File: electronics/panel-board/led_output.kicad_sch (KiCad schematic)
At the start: 12 parts, among them J17 Conn_02x04_Odd_Even, U11 74HCT245

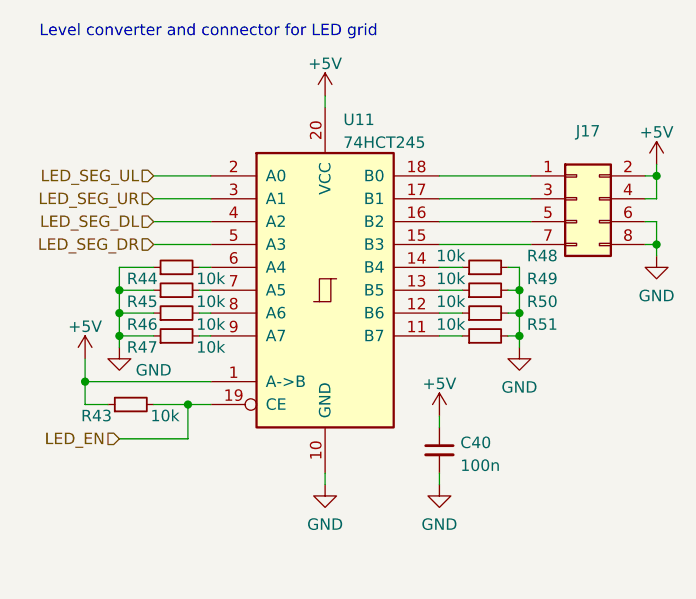
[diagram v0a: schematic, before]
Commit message: Update PadBUS standard
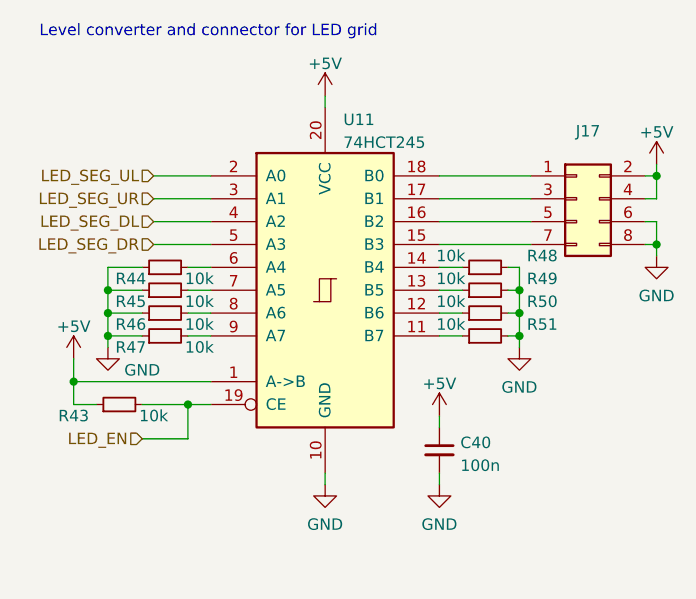
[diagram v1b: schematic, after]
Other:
- moved on the sheet: R43, R44, R45, R46, R47

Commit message: Pre LED grid changes
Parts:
- added H3, H4: MountingHole_Pad, MountingHole:MountingHole_3.2mm_M3_Pad, symbol Mechanical:MountingHole_Pad
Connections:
- no-connect marks 0 -> 2
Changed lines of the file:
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@@
   (junction (at 74.93 46.99) (diameter 0) (color 0 0 0 0)
   )
+  (no_connect (at 25.4 76.2))
+  (no_connect (at 33.02 76.2))
   (wire (pts (xy 74.93 41.91) (xy 74.93 44.45))
     (stroke (width 0) (type default) (color 0 0 0 0))
@@
     (pin "2")
   )
+  (symbol (lib_id "Mechanical:MountingHole_Pad") (at 33.02 73.66 0) (mirror y) (unit 1)
+    (in_bom yes) (on_board yes) (fields_autoplaced)
+    (property "Reference" "H4" (id 0) (at 30.48 71.5553 0)
+      (effects (font (size 1.27 1.27)) (justify left))
+    )
+    (property "Value" "MountingHole_Pad" (id 1) (at 30.48 74.0922 0)
+      (effects (font (size 1.27 1.27)) (justify left) hide)
+    )
+    (property "Footprint" "MountingHole:MountingHole_3.2mm_M3_Pad" (id 2) (at 33.02 73.66 0)
+      (effects (font (size 1.27 1.27)) hide)
+    )
+    (property "Datasheet" "~" (id 3) (at 33.02 73.66 0)
+      (effects (font (size 1.27 1.27)) hide)
+    )
+    (pin "1")
+  )
   (symbol (lib_id "power:GND") (at 90.17 40.64 0) (unit 1)
     (in_bom yes) (on_board yes) (fields_autoplaced)
@@
     )
     (property "Datasheet" "" (id 3) (at 53.34 22.86 0)
+      (effects (font (size 1.27 1.27)) hide)
+    )
+    (pin "1")
+  )
+  (symbol (lib_id "Mechanical:MountingHole_Pad") (at 25.4 73.66 0) (mirror y) (unit 1)
+    (in_bom yes) (on_board yes) (fields_autoplaced)
+    (property "Reference" "H3" (id 0) (at 22.86 71.5553 0)
+      (effects (font (size 1.27 1.27)) (justify left))
+    )
+    (property "Value" "MountingHole_Pad" (id 1) (at 22.86 74.0922 0)
+      (effects (font (size 1.27 1.27)) (justify left) hide)
+    )
+    (property "Footprint" "MountingHole:MountingHole_3.2mm_M3_Pad" (id 2) (at 25.4 73.66 0)
+      (effects (font (size 1.27 1.27)) hide)
+    )
+    (property "Datasheet" "~" (id 3) (at 25.4 73.66 0)
       (effects (font (size 1.27 1.27)) hide)
     )
@@
     (pin "1")
   )
+  (sheet_instances
+    (path "/" (page "1"))
+  )
+  (symbol_instances
+    (path "/461e0b65-0fb8-4924-9a86-ecf473ffba58"
+      (reference "#PWR096") (unit 1) (value "+5V") (footprint "")
+    )
+    (path "/277de0f0-3211-4bd1-b44f-edce4479dc5e"
+      (reference "#PWR097") (unit 1) (value "GND") (footprint "")
+    )
+    (path "/9244ab2d-6ee8-49fa-9ad3-e2a4e003c7fc"
+      (reference "#PWR098") (unit 1) (value "+5V") (footprint "")
+    )
+    (path "/18e83fbf-8ee7-4c40-a225-e25221b68051"
+      (reference "#PWR099") (unit 1) (value "GND") (footprint "")
+    )
+    (path "/2f5e3d2b-d1ac-4ed0-925a-d1d741086e74"
+      (reference "#PWR0100") (unit 1) (value "+5V") (footprint "")
+    )
+    (path "/1a6bda49-61b3-4d06-ac42-bd2778460cec"
+      (reference "#PWR0101") (unit 1) (value "GND") (footprint "")
+    )
+    (path "/32735fec-a454-4083-a969-1c6caf13a039"
+      (reference "#PWR0102") (unit 1) (value "GND") (footprint "")
+    )
+    (path "/ef98ee5c-5e6d-4bb9-a299-aed4269ec334"
+      (reference "#PWR0103") (unit 1) (value "+5V") (footprint "")
+    )
+    (path "/8ed777de-8094-4ab3-bcee-f9d79b796a51"
+      (reference "#PWR0104") (unit 1) (value "GND") (footprint "")
+    )
+    (path "/ca6142fe-4e98-448d-8eb5-8dbcef3187c3"
+      (reference "C40") (unit 1) (value "100n") (footprint "Capacitor_SMD:C_0603_1608Metric")
+    )
+    (path "/be06eaf9-e59b-4cca-9a1a-d403de0fb6ac"
+      (reference "J17") (unit 1) (value "Conn_02x04_Odd_Even") (footprint "Connector_IDC:IDC-Header_2x04_P2.54mm_Vertical")
+    )
+    (path "/b79e35f8-cb90-4c40-a467-833e9e1e6874"
+      (reference "R43") (unit 1) (value "10k") (footprint "Resistor_SMD:R_0603_1608Metric")
+    )
+    (path "/0d3ef995-8c12-4bfe-ab5d-517833ba9813"
+      (reference "R44") (unit 1) (value "10k") (footprint "Resistor_SMD:R_0603_1608Metric")
+    )
+    (path "/daa0c869-f76b-4c3d-808b-d79280f0317c"
+      (reference "R45") (unit 1) (value "10k") (footprint "Resistor_SMD:R_0603_1608Metric")
+    )
+    (path "/ae3f2756-756a-4bf9-a176-b6f9fc146d86"
+      (reference "R46") (unit 1) (value "10k") (footprint "Resistor_SMD:R_0603_1608Metric")
+    )
+    (path "/71d70e52-25fd-4513-ac6a-555ae367ed03"
+      (reference "R47") (unit 1) (value "10k") (footprint "Resistor_SMD:R_0603_1608Metric")
+    )
+    (path "/1277724d-44b8-4596-89b4-ea1562a8e479"
+      (reference "R48") (unit 1) (value "10k") (footprint "Resistor_SMD:R_0603_1608Metric")
+    )
+    (path "/524fbb20-d3c2-4531-8f54-a1370d04835b"
+      (reference "R49") (unit 1) (value "10k") (footprint "Resistor_SMD:R_0603_1608Metric")
+    )
+    (path "/250683ea-e760-419e-883e-578659661b66"
+      (reference "R50") (unit 1) (value "10k") (footprint "Resistor_SMD:R_0603_1608Metric")
+    )
+    (path "/bcb650d9-eced-4e1f-aeb5-548a6335ffd5"
+      (reference "R51") (unit 1) (value "10k") (footprint "Resistor_SMD:R_0603_1608Metric")
+    )
+    (path "/5dc313ee-530d-4194-b50e-61b805755b2f"
+      (reference "U11") (unit 1) (value "74HCT245") (footprint "Package_SO:TSSOP-20_4.4x6.5mm_P0.65mm")
+    )
+  )
 )
